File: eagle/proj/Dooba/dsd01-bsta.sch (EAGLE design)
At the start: 63 parts, among them J1 PWRJACK5521, J8 ARJC02-111008B, P1 DIO, P2 CKI-CKO, P3 NOT, P4 RDY, P5 PWR(VIN-GND-RST), P6 SWD_CORE(SWCLK-SWDIO-GND), P7 SWD_CORE(SWCLK-SWDIO-GND), P8 SWD(GND-RST)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

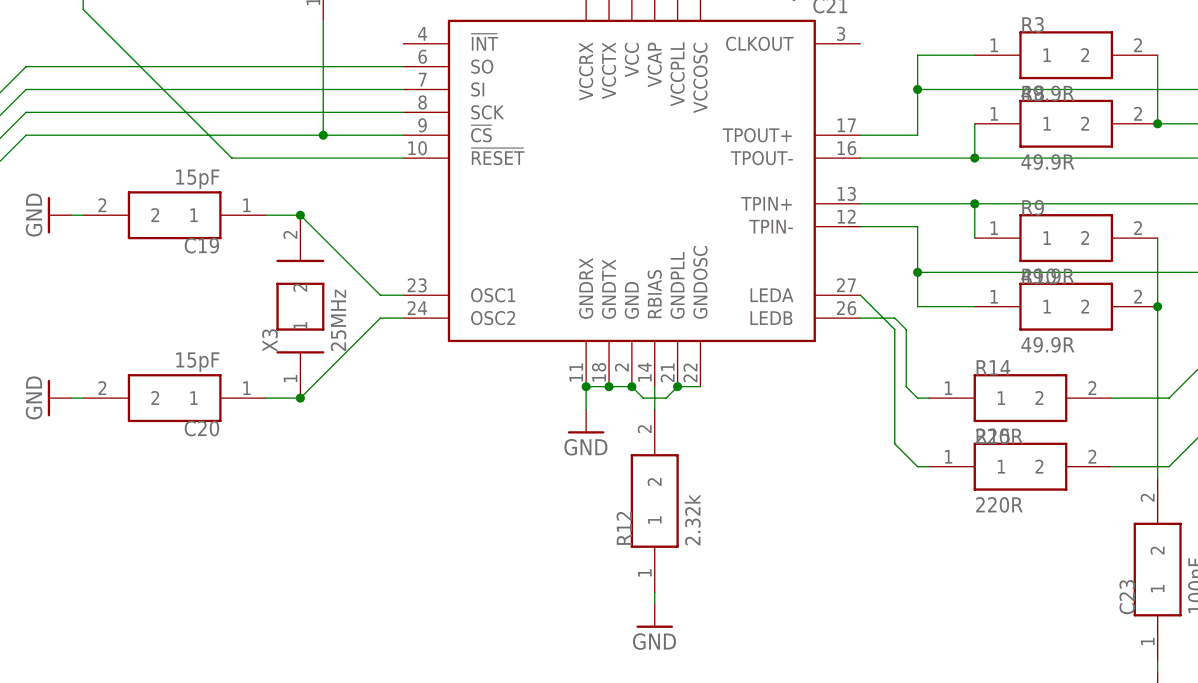
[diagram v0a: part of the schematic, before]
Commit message: Completed DSY01 & DSD01-BSTA boards
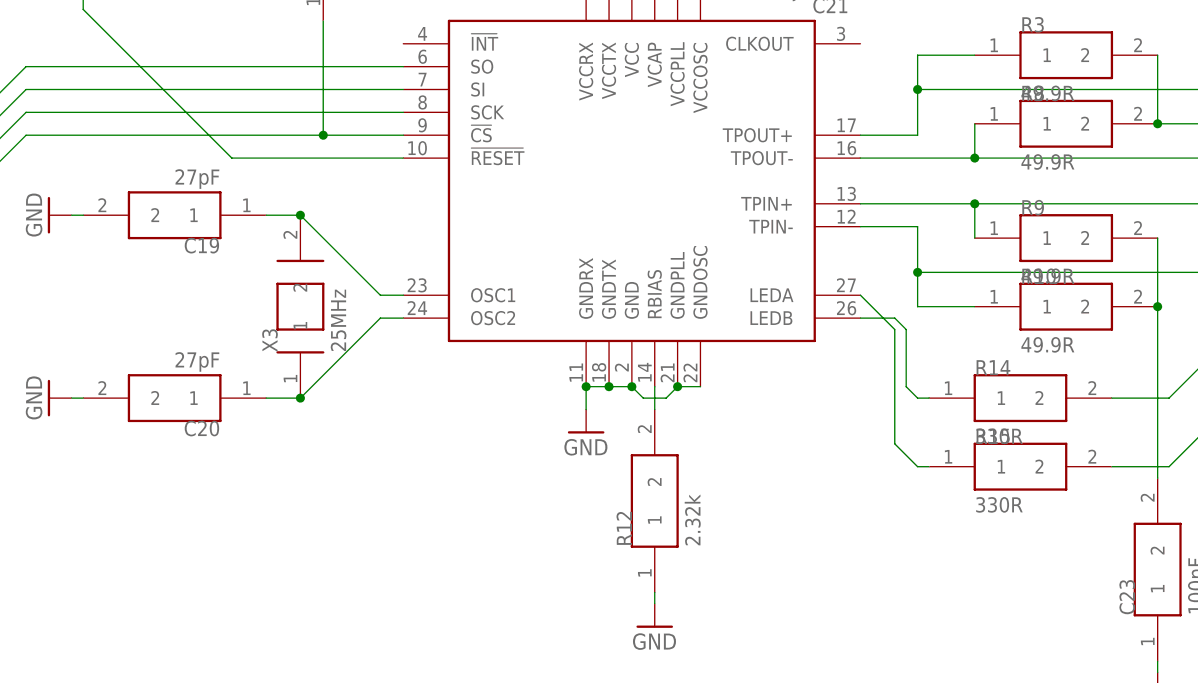
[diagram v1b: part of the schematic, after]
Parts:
- C19, C20: value 15pF -> 27pF
- R14, R15: value 220R -> 330R
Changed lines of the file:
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@@
 <part name="U13" library="pahoo" deviceset="ENC28J60/SS" device=""/>
 <part name="X3" library="dooba" deviceset="XTAL" device="SMD-5X32" value="25MHz"/>
-<part name="C19" library="dooba" deviceset="CAP" device="0805" value="15pF"/>
-<part name="C20" library="dooba" deviceset="CAP" device="0805" value="15pF"/>
+<part name="C19" library="dooba" deviceset="CAP" device="0805" value="27pF"/>
+<part name="C20" library="dooba" deviceset="CAP" device="0805" value="27pF"/>
 <part name="J8" library="pahoo" deviceset="ARJC02-111008B" device=""/>
 <part name="C21" library="dooba" deviceset="CAP" device="0805" value="100nF"/>
@@
 <part name="R12" library="dooba" deviceset="RES" device="0805" value="2.32k"/>
 <part name="R13" library="dooba" deviceset="RES" device="0805" value="10k"/>
-<part name="R14" library="dooba" deviceset="RES" device="0805" value="220R"/>
-<part name="R15" library="dooba" deviceset="RES" device="0805" value="220R"/>
+<part name="R14" library="dooba" deviceset="RES" device="0805" value="330R"/>
+<part name="R15" library="dooba" deviceset="RES" device="0805" value="330R"/>
 <part name="GND21" library="supply1" deviceset="GND" device=""/>
 <part name="GND22" library="supply1" deviceset="GND" device=""/>
